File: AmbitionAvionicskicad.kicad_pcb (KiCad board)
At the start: 4 copper layers, 19 parts, among them J11 ADA-SD READ/WRITE, J12 UART to Pi, J13 PowerToPi, J3 Batt_GND, J4 Batt_Vin

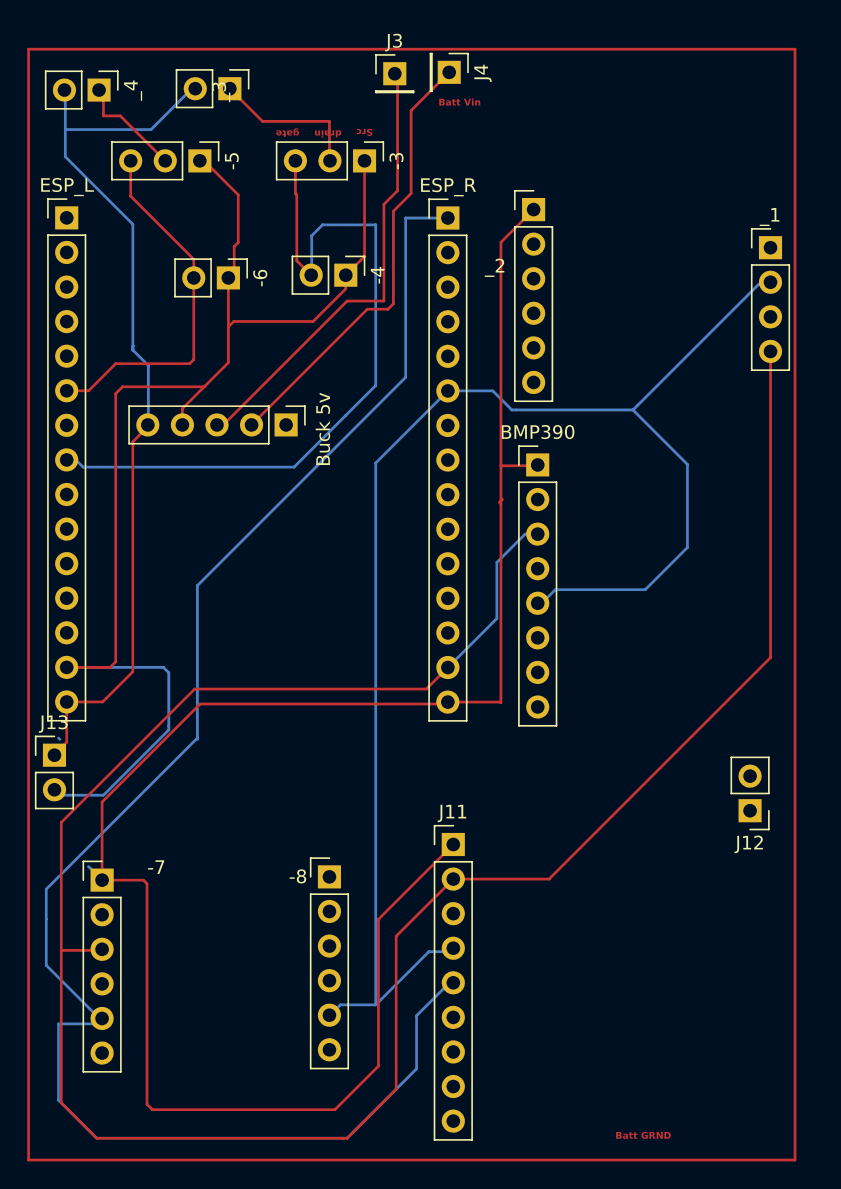
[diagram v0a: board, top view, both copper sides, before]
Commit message: Pruned connections, Added written documentation on board
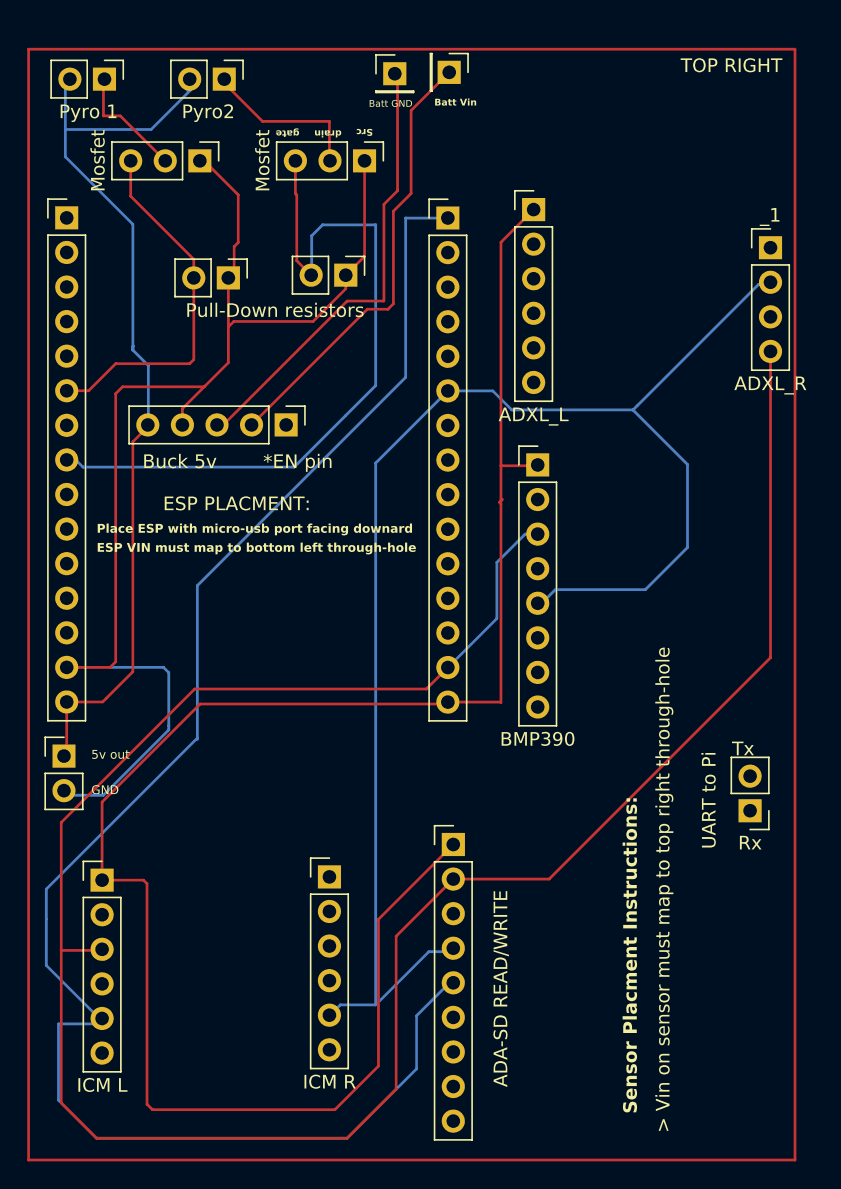
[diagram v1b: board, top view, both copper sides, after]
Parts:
- -6: value Pull-Down resistor -> Pull-Down resistors
- Batt GND: renamed from J3
- Buck 5v: value Buck. Out+ leftmost -> *EN pin
- ESP PLACMENT: : renamed from J13
- Pyro 1: renamed from _4; value Pyro1 -> (none)
- moved Pyro 1 0.89 mm to (90.0, 23.2)
- moved _3 0.81 mm to (98.8, 23.2)
- moved ESP PLACMENT:  0.70 mm to (87.0, 72.9)
- renumbered J12 to Rx
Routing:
- net /CS_4: track 106.2 -> 86.0 mm
- net /MOSI: track 194.5 -> 179.2 mm
- net /GND_2: track 95.6 -> 94.0 mm
- net (no net): track 445.4 -> 444.4 mm
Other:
- board text added: "5v out"
- board text added: "> Vin on sensor must map to top right through-hole"
- board text added: "ESP VIN must map to bottom left through-hole"
- board text added: "GND"
- board text added: "Place ESP with micro-usb port facing downard"
- board text added: "Sensor Placment Instructions:"
- board text added: "TOP RIGHT"
- board text removed: "Batt GRND"
